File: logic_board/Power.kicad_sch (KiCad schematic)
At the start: 19 parts, among them J3 USB_C_Receptacle_USB2.0_16P, J5 Battery, Q1 BSS138, SW5 SW_SPDT, U3 BQ25185DLHR, U4 AP2112K-3.3, U5 USBLC6-2SC6

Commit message: Fix JLCPCB issues
- Use fabrication toolkit plugin to fix compnent orientations.
- Add part numbers to all components
- Manually fix some footprint rotation issues and incorrect origins.
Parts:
- C23, C25: LCSC Part Number (none) -> C15849
- C24: LCSC Part Number (none) -> C15850
- C26: LCSC Part Number (none) -> C23630
- D6: LCSC Part Number (none) -> C22466350
- R1, R18: LCSC Part Number (none) -> C25804
- R17: LCSC Part Number (none) -> C862232
- R23: LCSC Part Number (none) -> C25803
- R8, R9: LCSC Part Number (none) -> C23186
- SW5: now in the parts list
- U5: FT Rotation Offset (none) -> -90
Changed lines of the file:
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@@
 			)
 		)
-		(property "LCSC part number" ""
+		(property "LCSC Part Number" "C23186"
 			(at 57.15 44.45 90)
 			(effects
@@
 			)
 		)
-		(property "LCSC part number" ""
+		(property "LCSC Part Number" "C25803"
 			(at 143.51 104.14 90)
 			(effects
@@
 			)
 		)
-		(property "LCSC part number" ""
-			(at 157.48 104.14 0)
-			(effects
-				(font
-					(size 1.27 1.27)
-				)
-				(hide yes)
-			)
-		)
 		(pin "2"
 		)
@@
 			)
 		)
-		(property "LCSC part number" ""
+		(property "LCSC Part Number" "C23630"
 			(at 172.72 109.22 0)
 			(effects
@@
 			)
 		)
-		(property "LCSC part number" ""
+		(property "LCSC Part Number" "C22466350"
 			(at 130.81 111.76 90)
 			(effects
@@
 			)
 		)
-		(property "LCSC part number" ""
-			(at 140.97 138.43 0)
-			(effects
-				(font
-					(size 1.27 1.27)
-				)
-				(hide yes)
-			)
-		)
 		(pin "3"
 		)
@@
 			)
 		)
-		(property "LCSC part number" ""
+		(property "LCSC Part Number" "C25804"
 			(at 161.29 60.96 0)
 			(effects
@@
 			)
 		)
-		(property "LCSC part number" ""
-			(at 181.61 45.72 0)
-			(effects
-				(font
-					(size 1.27 1.27)
-				)
-				(hide yes)
-			)
-		)
 		(pin "3"
 		)
@@
 			)
 		)
-		(property "LCSC part number" ""
+		(property "LCSC Part Number" "C25804"
 			(at 205.74 43.18 90)
 			(effects
@@
 			)
 		)
-		(property "LCSC part number" ""
+		(property "LCSC Part Number" "C862232"
 			(at 156.21 60.96 0)
 			(effects
@@
 			)
 		)
-		(property "LCSC part number" ""
+		(property "LCSC Part Number" "C15849"
 			(at 208.28 60.96 0)
 			(effects
@@
 			)
 		)
-		(property "LCSC part number" ""
-			(at 220.98 52.07 0)
-			(effects
-				(font
-					(size 1.27 1.27)
-				)
-				(hide yes)
-			)
-		)
 		(pin "2"
 		)
@@
 			)
 		)
-		(property "LCSC part number" ""
+		(property "LCSC Part Number" "C23186"
 			(at 57.15 41.91 90)
 			(effects
@@
 			)
 		)
-		(property "LCSC part number" ""
+		(property "LCSC Part Number" "C15850"
 			(at 86.36 109.22 0)
 			(effects
@@
 			)
 		)
-		(property "LCSC part number" ""
+		(property "FT Rotation Offset" "-90"
 			(at 74.93 52.07 0)
 			(effects
@@
 			)
 		)
-		(property "LCSC part number" ""
+		(property "LCSC Part Number" "C15849"
 			(at 106.68 45.72 0)
 			(effects
@@
 		)
 		(property "LCSC Part Number" "C165948"
-			(at 36.83 52.07 0)
-			(effects
-				(font
-					(size 1.27 1.27)
-				)
-				(hide yes)
-			)
-		)
-		(property "LCSC part number" ""
 			(at 36.83 52.07 0)
 			(effects
@@
 		(unit 1)
 		(exclude_from_sim no)
-		(in_bom no)
+		(in_bom yes)
 		(on_board yes)
 		(dnp no)
@@
 			)
 		)
-		(property "LCSC part number" ""
-			(at 109.22 127 0)
-			(effects
-				(font
-					(size 1.27 1.27)
-				)
-				(hide yes)
-			)
-		)
 		(pin "3"
 		)
@@
 			(at 99.06 45.72 90)
 			(effects
-				(font
-					(size 1.27 1.27)
-				)
-				(hide yes)
-			)
-		)
-		(property "LCSC part number" ""
-			(at 99.06 45.72 90)
-			(effects

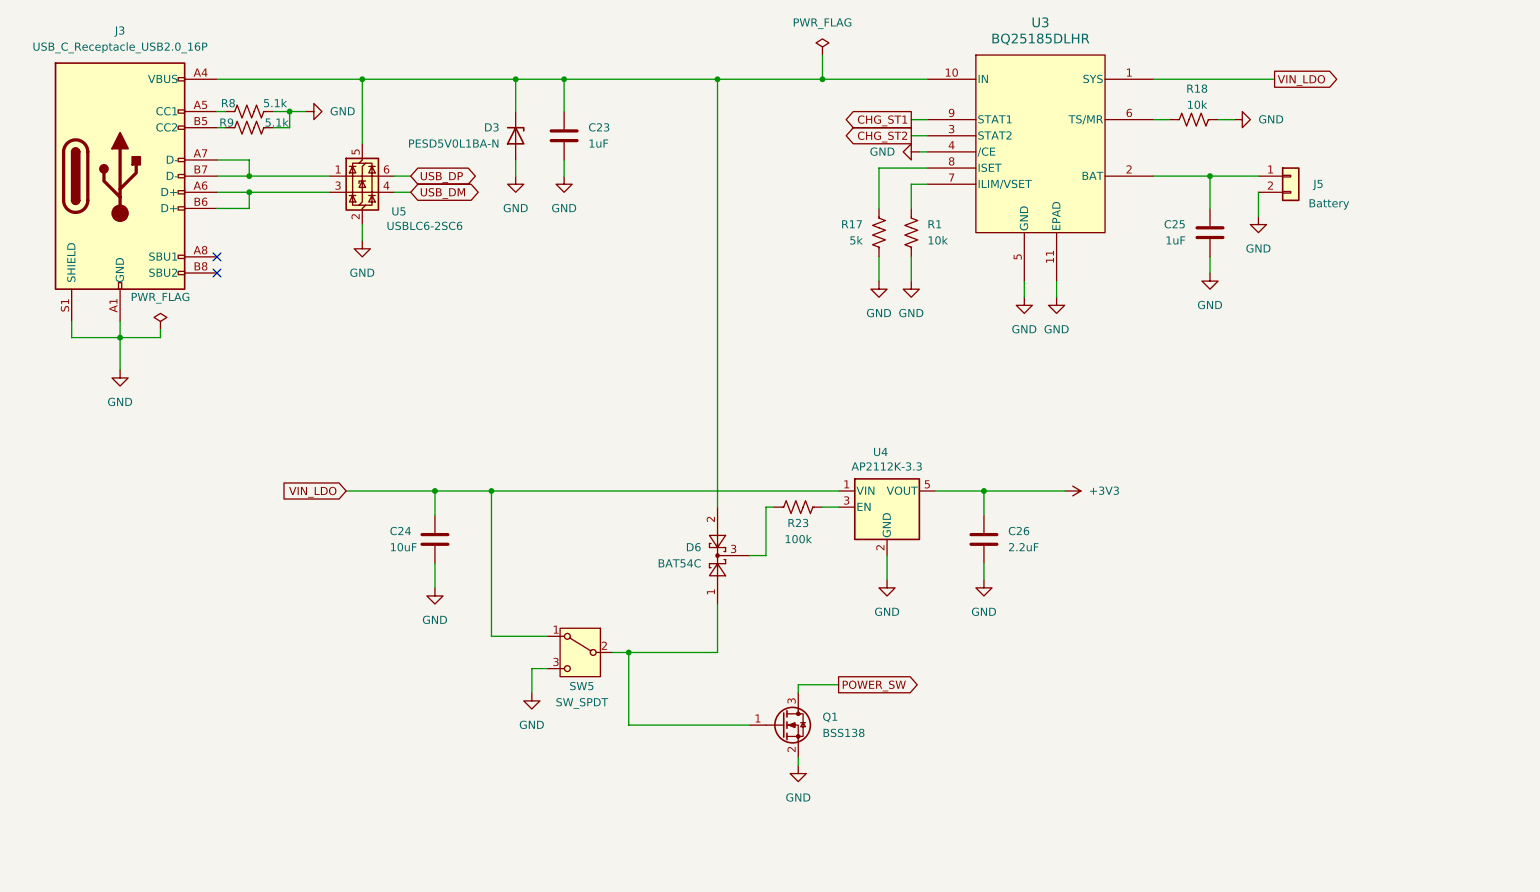
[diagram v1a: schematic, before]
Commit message: Switch to buck power converter
There's a small battery life win, but some basic calculations suggested the LDO would get pretty hot.
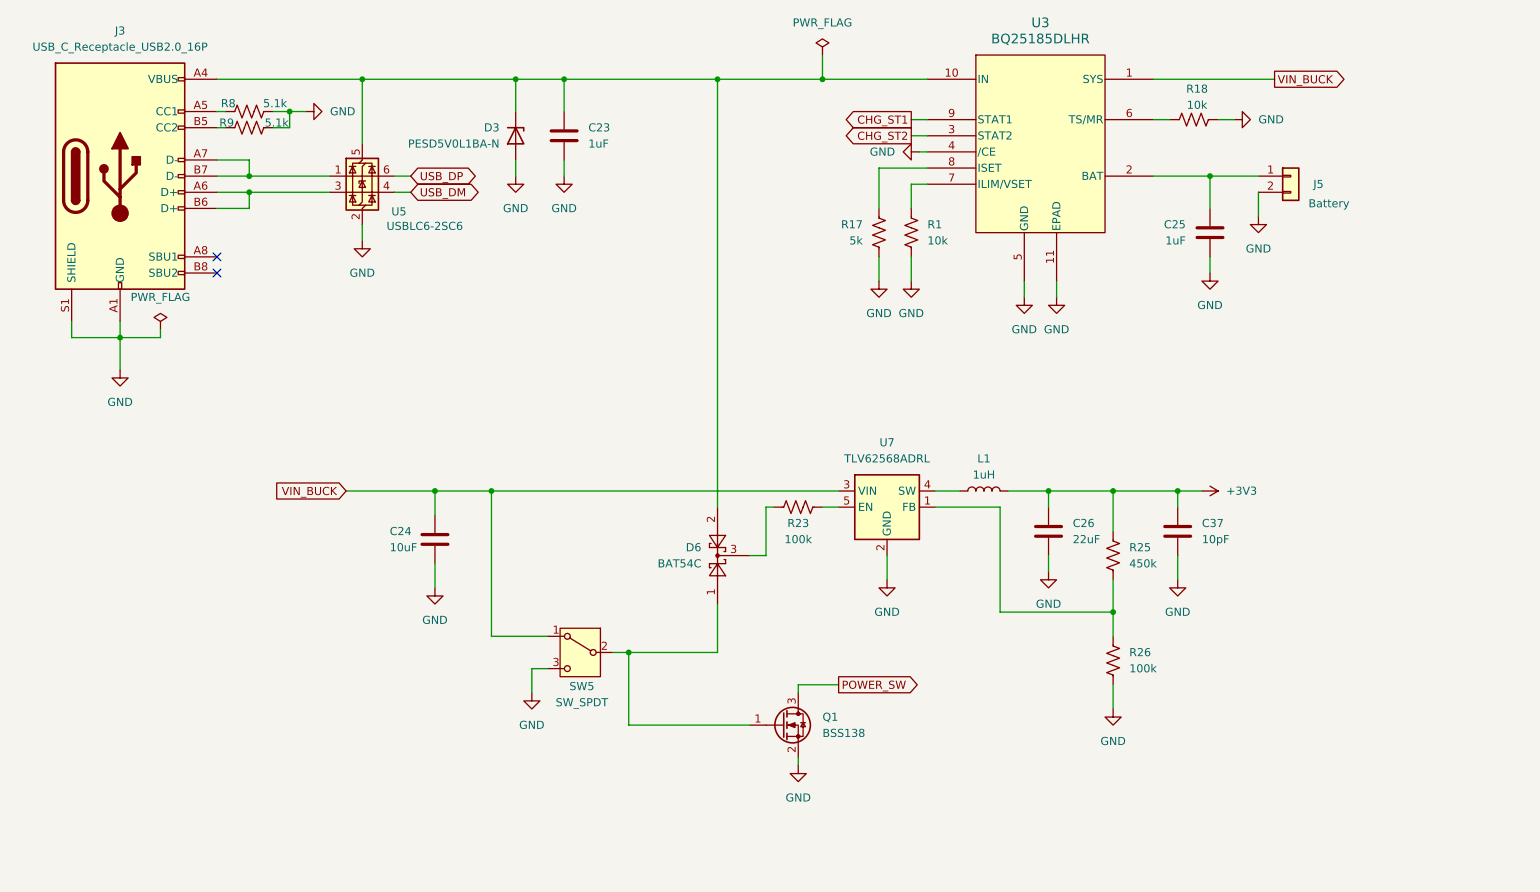
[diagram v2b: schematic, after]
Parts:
- removed U4: AP2112K-3.3, Package_TO_SOT_SMD:SOT-23-5, symbol Regulator_Linear:AP2112K-3.3
- added C37: 10pF, Capacitor_SMD:C_0603_1608Metric, symbol Device:C
- added L1: 1uH, Inductor_SMD:L_APV_ANR4010, symbol Device:L
- added R25: 450k, Resistor_SMD:R_0603_1608Metric, symbol Device:R_US
- added R26: 100k, Resistor_SMD:R_0603_1608Metric, symbol Device:R_US
- added U7: TLV62568ADRL, Package_TO_SOT_SMD:SOT-563, symbol Regulator_Switching:TLV62568ADRL
- C26: value 2.2uF -> 22uF; footprint Capacitor_SMD:C_0603_1608Metric -> Capacitor_SMD:C_0805_2012Metric; LCSC Part Number C23630 -> (none)
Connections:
- net +3V3: now also C37.1, L1.2, R25.1
- net GND: now also C37.2, R26.2, U7.2 (GND)
- net at R23.2: now also U7.5 (EN)
- net VIN_LDO renamed VIN_BUCK
- net VIN_BUCK: now also U7.3 (VIN)
- new net: L1.1, U7.4 (SW)
- new net: R25.2, R26.1, U7.1 (FB)
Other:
- moved on the sheet: C26

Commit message: Fix some PCB issues
TVS diodes had wrong footprint
U5 was rotated 180 degrees in CPL file.
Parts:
- C26: LCSC Part Number (none) -> C45783
- C37: LCSC Part Number (none) -> C1634
- D3: footprint Diode_SMD:D_SOD-882 -> Diode_SMD:D_SOD-323
- L1: LCSC Part Number (none) -> C135261
- Q1: LCSC Part Number (none) -> C7420339
- R26: LCSC Part Number (none) -> C25803
- U5: FT Rotation Offset -90 -> 90
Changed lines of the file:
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@@
 			)
 		)
-		(property "LCSC Part Number" ""
+		(property "LCSC Part Number" "C1634"
 			(at 203.2 107.95 0)
 			(effects
@@
 			)
 		)
+		(property "LCSC Part Number" "C135261"
+			(at 172.72 101.6 90)
+			(effects
+				(font
+					(size 1.27 1.27)
+				)
+				(hide yes)
+			)
+		)
 		(pin "1"
 		)
@@
 			)
 		)
-		(property "LCSC Part Number" ""
+		(property "LCSC Part Number" "C45783"
 			(at 182.88 107.95 0)
 			(effects
@@
 			)
 		)
+		(property "LCSC Part Number" "C7420339"
+			(at 140.97 138.43 0)
+			(effects
+				(font
+					(size 1.27 1.27)
+				)
+				(hide yes)
+			)
+		)
 		(pin "3"
 		)
@@
 			)
 		)
+		(property "LCSC Part Number" "C25803"
+			(at 193.04 128.27 0)
+			(effects
+				(font
+					(size 1.27 1.27)
+				)
+				(hide yes)
+			)
+		)
 		(pin "1"
 		)
@@
 			)
 		)
-		(property "FT Rotation Offset" "-90"
+		(property "FT Rotation Offset" "90"
 			(at 74.93 52.07 0)
 			(effects
@@
 			)
 		)
-		(property "Footprint" "Diode_SMD:D_SOD-882"
+		(property "Footprint" "Diode_SMD:D_SOD-323"
 			(at 93.98 45.72 0)
 			(effects

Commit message: Add test points, schematic annotations
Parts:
- added TP4, TP5, TP6, TP7: TestPoint, TestPoint:TestPoint_Pad_D1.0mm, symbol Connector:TestPoint
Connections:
- net +3V3: now also TP6.1
- net GND: now also TP7.1
- net VIN_BUCK: now also TP5.1
- net at C23.1, D3.1 (K), D6.2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: now also TP4.1
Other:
- note added: "Power Switch"
- moved on the sheet: C23, C24, C25, C26, C37, D3, D6, J3, J5, L1, Q1, R1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

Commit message: Ferrite for codec AVDD was incorrectly placed
It was in parallel the chip instead of in series with the source.
Also fixed ERC warning by adding power flag after buck inductor.
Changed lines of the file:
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@@
 	)
 	(junction
+		(at 193.04 113.03)
+		(diameter 0)
+		(color 0 0 0 0)
+	)
+	(junction
 		(at 92.71 113.03)
 		(diameter 0)
@@
 	(wire
 		(pts
+			(xy 193.04 113.03) (xy 199.39 113.03)
+		)
+		(stroke
+			(width 0)
+			(type default)
+		)
+	)
+	(wire
+		(pts
 			(xy 153.67 115.57) (xy 156.21 115.57)
 		)
@@
 	(wire
 		(pts
+			(xy 193.04 105.41) (xy 193.04 113.03)
+		)
+		(stroke
+			(width 0)
+			(type default)
+		)
+	)
+	(wire
+		(pts
 			(xy 107.95 140.97) (xy 107.95 144.78)
 		)
@@
 	(wire
 		(pts
-			(xy 189.23 113.03) (xy 199.39 113.03)
+			(xy 189.23 113.03) (xy 193.04 113.03)
 		)
 		(stroke
@@
 					(unit 1)
 				)
+			)
+		)
+	)
+	(symbol
+		(lib_id "power:PWR_FLAG")
+		(at 193.04 105.41 0)
+		(unit 1)
+		(exclude_from_sim no)
+		(in_bom yes)
+		(on_board yes)
+		(dnp no)
+		(fields_autoplaced yes)
+		(property "Reference" "#FLG04"
+			(at 193.04 103.505 0)
+			(effects
+				(font
+					(size 1.27 1.27)
+				)
+				(hide yes)
+			)
+		)
+		(property "Value" "PWR_FLAG"
+			(at 193.04 100.33 0)
+			(effects
+				(font
+					(size 1.27 1.27)
+				)
+			)
+		)
+		(property "Footprint" ""
+			(at 193.04 105.41 0)
+			(effects
+				(font
+					(size 1.27 1.27)
+				)
+				(hide yes)
+			)
+		)
+		(property "Datasheet" "~"
+			(at 193.04 105.41 0)
+			(effects
+				(font
+					(size 1.27 1.27)
+				)
+				(hide yes)
+			)
+		)
+		(property "Description" "Special symbol for telling ERC where power comes from"
+			(at 193.04 105.41 0)
+			(effects
+				(font
+					(size 1.27 1.27)
+				)
+				(hide yes)
+			)
+		)
+		(pin "1"
+		)
+		(instances
+			(project ""
+				(path "/b7b37fe1-b409-497a-9440-d94d882f6459/78b9c77c-6b0c-47f1-b5e8-ea96354c74d6"
+					(reference "#FLG04")
+					(unit 1)
+				)

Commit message: Set max charge current appropriately with resistor values.
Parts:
- R1: value 10k -> 18k; LCSC Part Number C25804 -> (none)
- R17: value 5k -> 600; LCSC Part Number C862232 -> (none)
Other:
- note added: "Max charge current/ input current: 400mA"
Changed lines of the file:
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@@
 	(generator_version "9.0")
 	(paper "A4")
+	(text "Max charge current/\ninput current: 400mA"
+		(exclude_from_sim no)
+		(at 150.876 67.056 0)
+		(effects
+			(font
+				(size 1.27 1.27)
+			)
+		)
+	)
 	(text "Power Switch"
 		(exclude_from_sim no)
@@
 			)
 		)
-		(property "Value" "10k"
+		(property "Value" "18k"
 			(at 170.18 73.6599 0)
 			(effects
@@
 			)
 		)
-		(property "LCSC Part Number" "C25804"
+		(property "LCSC Part Number" ""
 			(at 167.64 72.39 0)
 			(effects
@@
 			)
 		)
-		(property "Value" "5k"
+		(property "Value" "600"
 			(at 160.02 73.6599 0)
 			(effects
@@
 			)
 		)
-		(property "LCSC Part Number" "C862232"
+		(property "LCSC Part Number" ""
 			(at 162.56 72.39 0)
 			(effects

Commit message: Change value of buck converter FB divider registers
First reduce the values for less noise susceptibility and
jitter, but also pick standard E24 values.
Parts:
- R25: value 450k -> 215k
- R26: value 100k -> 47k; LCSC Part Number C25803 -> (none)
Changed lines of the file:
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@@
 			)
 		)
-		(property "Value" "100k"
+		(property "Value" "47k"
 			(at 201.93 140.9699 0)
 			(effects
@@
 			)
 		)
-		(property "LCSC Part Number" "C25803"
+		(property "LCSC Part Number" ""
 			(at 199.39 139.7 0)
 			(effects
@@
 			)
 		)
-		(property "Value" "450k"
+		(property "Value" "215k"
 			(at 201.93 124.4599 0)
 			(effects

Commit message: Lay out power supply section.
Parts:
- removed TP4, TP5: TestPoint, TestPoint:TestPoint_Pad_D1.0mm, symbol Connector:TestPoint
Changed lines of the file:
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@@
 	)
 	(junction
-		(at 96.52 48.26)
-		(diameter 0)
-		(color 0 0 0 0)
-	)
-	(junction
 		(at 123.19 138.43)
 		(diameter 0)
@@
 	)
 	(junction
-		(at 214.63 48.26)
-		(diameter 0)
-		(color 0 0 0 0)
-	)
-	(junction
 		(at 199.39 113.03)
 		(diameter 0)
@@
 	(wire
 		(pts
-			(xy 96.52 41.91) (xy 96.52 48.26)
-		)
-		(stroke
-			(width 0)
-			(type default)
-		)
-	)
-	(wire
-		(pts
 			(xy 193.04 113.03) (xy 199.39 113.03)
 		)
@@
 	(wire
 		(pts
-			(xy 96.52 48.26) (xy 105.41 48.26)
+			(xy 81.28 48.26) (xy 105.41 48.26)
 		)
 		(stroke
@@
 	(wire
 		(pts
-			(xy 205.74 48.26) (xy 214.63 48.26)
+			(xy 205.74 48.26) (xy 224.79 48.26)
 		)
 		(stroke
@@
 	(wire
 		(pts
-			(xy 214.63 48.26) (xy 224.79 48.26)
-		)
-		(stroke
-			(width 0)
-			(type default)
-		)
-	)
-	(wire
-		(pts
 			(xy 92.71 113.03) (xy 92.71 116.84)
 		)
@@
 	(wire
 		(pts
-			(xy 214.63 39.37) (xy 214.63 48.26)
-		)
-		(stroke
-			(width 0)
-			(type default)
-		)
-	)
-	(wire
-		(pts
 			(xy 163.83 123.19) (xy 163.83 127)
 		)
@@
 	(wire
 		(pts
-			(xy 81.28 48.26) (xy 96.52 48.26)
-		)
-		(stroke
-			(width 0)
-			(type default)
-		)
-	)
-	(wire
-		(pts
 			(xy 171.45 115.57) (xy 181.61 115.57)
 		)
@@
 	)
 	(symbol
-		(lib_id "Connector:TestPoint")
-		(at 96.52 41.91 0)
-		(unit 1)
-		(exclude_from_sim no)
-		(in_bom yes)
-		(on_board yes)
-		(dnp no)
-		(fields_autoplaced yes)
-		(property "Reference" "TP4"
-			(at 99.06 37.3379 0)
-			(effects
-				(font
-					(size 1.27 1.27)
-				)
-				(justify left)
-			)
-		)
-		(property "Value" "TestPoint"
-			(at 99.06 39.8779 0)
-			(effects
-				(font
-					(size 1.27 1.27)
-				)
-				(justify left)
-				(hide yes)
-			)
-		)
-		(property "Footprint" "TestPoint:TestPoint_Pad_D1.0mm"
-			(at 101.6 41.91 0)
-			(effects
-				(font
-					(size 1.27 1.27)
-				)
-				(hide yes)
-			)
-		)
-		(property "Datasheet" "~"
-			(at 101.6 41.91 0)
-			(effects
-				(font
-					(size 1.27 1.27)
-				)
-				(hide yes)
-			)
-		)
-		(property "Description" "test point"
-			(at 96.52 41.91 0)
-			(effects
-				(font
-					(size 1.27 1.27)
-				)
-				(hide yes)
-			)
-		)
-		(pin "1"
-		)
-		(instances
-			(project ""
-				(path "/b7b37fe1-b409-497a-9440-d94d882f6459/78b9c77c-6b0c-47f1-b5e8-ea96354c74d6"
-					(reference "TP4")
-					(unit 1)
-				)
-			)
-		)
-	)
-	(symbol
 		(lib_id "Device:R_US")
 		(at 149.86 115.57 90)
@@
 					(unit 1)
 				)
-			)
-		)
-	)
-	(symbol
-		(lib_id "Connector:TestPoint")
-		(at 214.63 39.37 0)
-		(unit 1)
-		(exclude_from_sim no)
-		(in_bom yes)
-		(on_board yes)
-		(dnp no)
-		(fields_autoplaced yes)
-		(property "Reference" "TP5"
-			(at 217.17 34.7979 0)
-			(effects
-				(font
-					(size 1.27 1.27)
-				)
-				(justify left)
-			)
-		)
-		(property "Value" "TestPoint"
-			(at 217.17 37.3379 0)
-			(effects
-				(font
-					(size 1.27 1.27)
-				)
-				(justify left)
-				(hide yes)
-			)
-		)
-		(property "Footprint" "TestPoint:TestPoint_Pad_D1.0mm"
-			(at 219.71 39.37 0)
-			(effects
-				(font
-					(size 1.27 1.27)
-				)
-				(hide yes)
-			)
-		)
-		(property "Datasheet" "~"
-			(at 219.71 39.37 0)
-			(effects
-				(font
-					(size 1.27 1.27)
-				)
-				(hide yes)
-			)
-		)
-		(property "Description" "test point"
-			(at 214.63 39.37 0)
-			(effects
-				(font
-					(size 1.27 1.27)
-				)
-				(hide yes)
-			)
-		)
-		(pin "1"
-		)
-		(instances
-			(project "logic_board"
-				(path "/b7b37fe1-b409-497a-9440-d94d882f6459/78b9c77c-6b0c-47f1-b5e8-ea96354c74d6"
-					(reference "TP5")
-					(unit 1)
-				)
